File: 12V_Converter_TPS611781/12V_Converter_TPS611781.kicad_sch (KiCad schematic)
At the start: 20 parts, among them M1 CSD17308Q3T, U1 LM51561DSSR

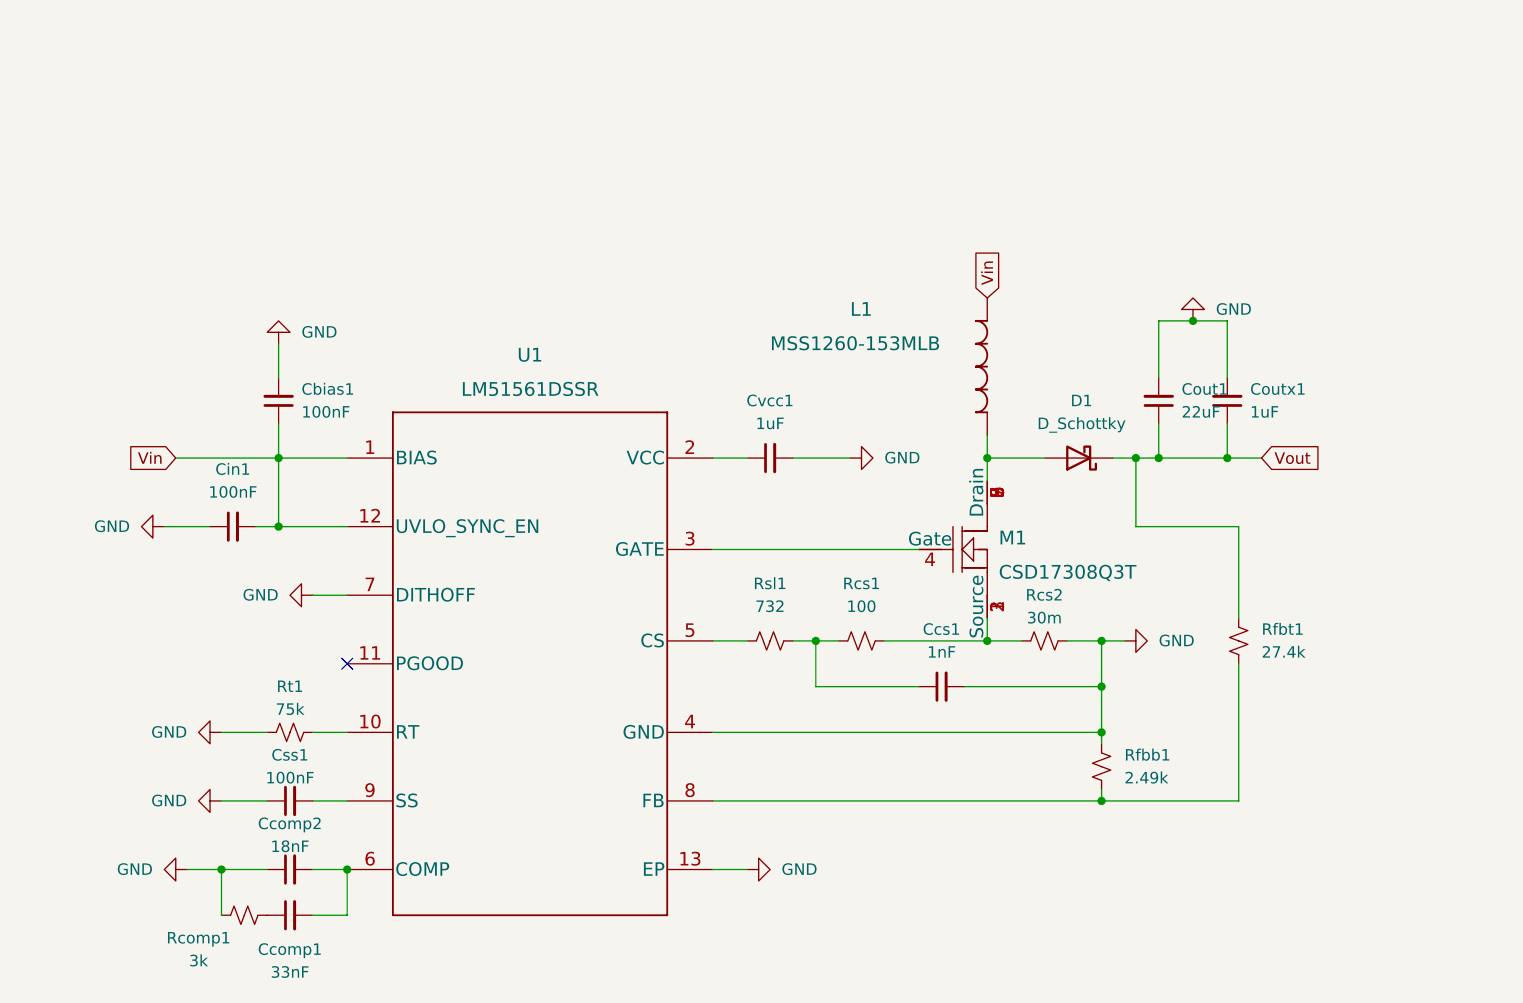
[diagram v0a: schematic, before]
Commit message: changed components
- changed inductor to be better resistance
- changed ic to be qfp instead of qfn
- changed N MOSFET to be 100V instead of 30V
- separated UVLO from Vin to allow for UVLO operation if needed (added external connect pin)
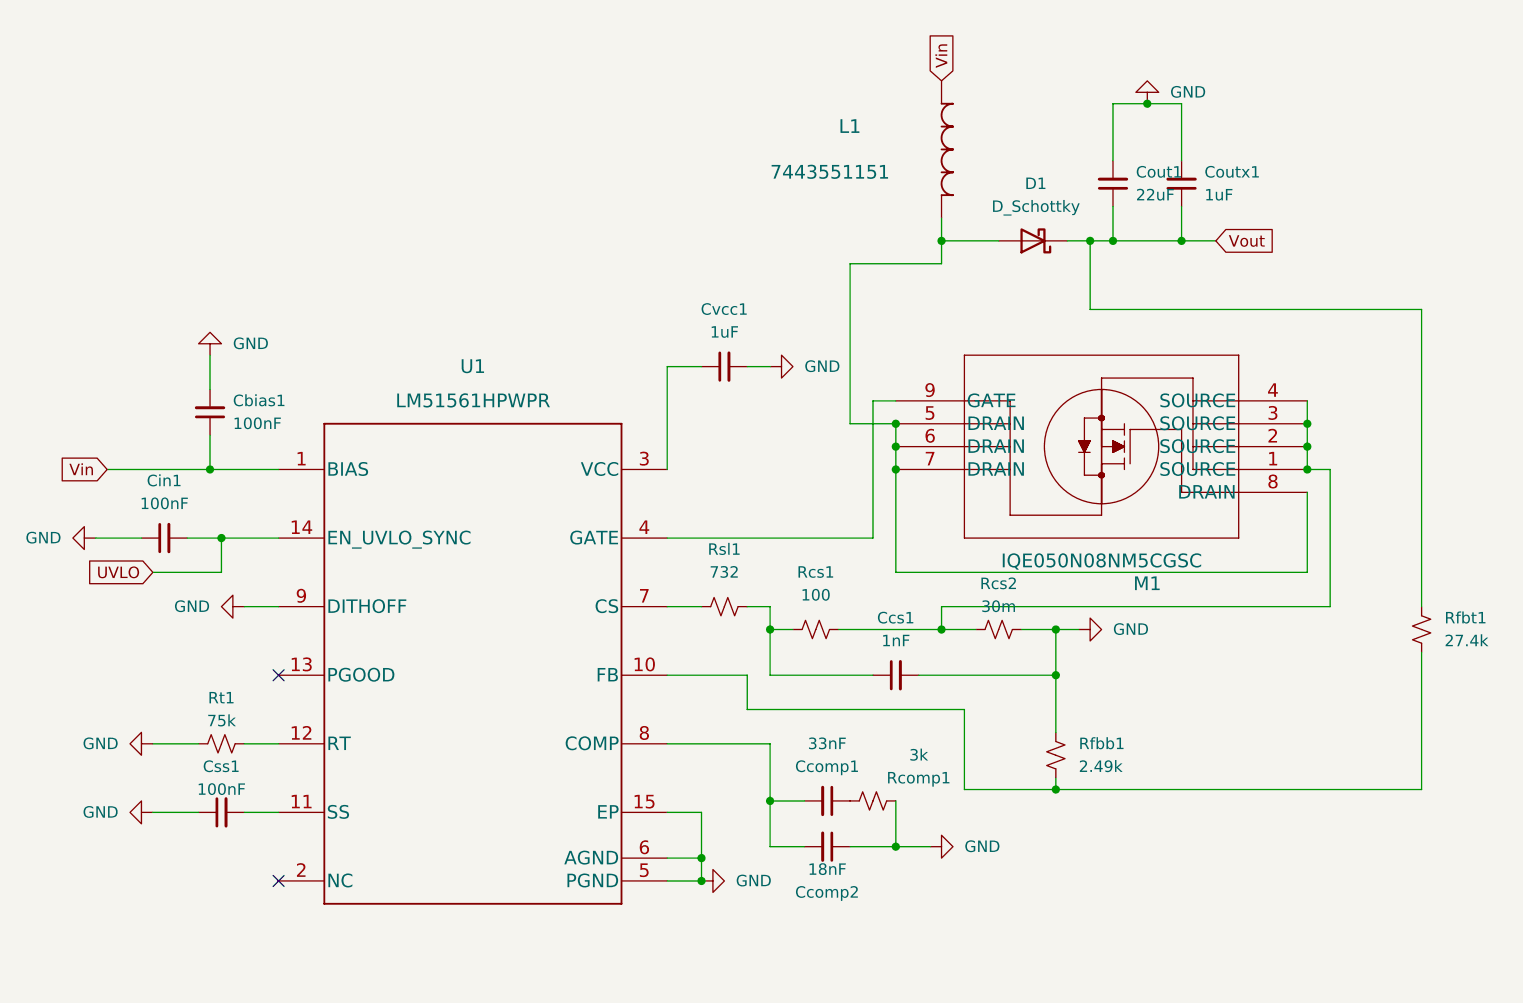
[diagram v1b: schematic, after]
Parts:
- removed L1: MSS1260-153MLB, MSS1260-153MLB:MSS1260-153MLB, symbol 2023-01-28_09-09-56:MSS1260-153MLB
- removed M1: CSD17308Q3T, CSD17308Q3T:CSD17308Q3T, symbol 2023-01-28_07-07-28:CSD17308Q3T
- removed U1: LM51561DSSR, LM51561DSSR:LM51561DSSR, symbol 2023-01-28_06-28-21:LM51561DSSR
- added L1: 7443551151, inductor:7443551151, symbol 2023-01-30_01-28-52:7443551151
- added M1: IQE050N08NM5CGSC, N MOSFET:IQE050N08NM5CGATMA1, symbol 2023-01-30_00-16-33:IQE050N08NM5CGATMA1
- added U1: LM51561HPWPR, IC:LM51561HPWPR, symbol 2023-01-29_23-53-00:LM51561HPWPR
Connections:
- net GND: now also U1.15 (EP), U1.5 (PGND), U1.6 (AGND), U1.9 (DITHOFF)
- net Vin: now also L1.2, U1.1 (BIAS); no longer Cin1.2
- net at Ccomp1.2, Ccomp2.2: now also U1.8 (COMP)
- net at Rfbb1.1, Rfbt1.1: now also U1.10 (FB)
- net at Rsl1.1: now also U1.7 (CS)
- net at Cvcc1.1: now also U1.3 (VCC)
- net at Rt1.2: now also U1.12 (RT)
- net at Css1.2: now also U1.11 (SS)
- net at D1.2 (A): now also L1.1, M1.5 (DRAIN), M1.6 (DRAIN), M1.7 (DRAIN), M1.8 (DRAIN)
- net at Rcs1.2, Rcs2.1: now also M1.1 (SOURCE), M1.2 (SOURCE), M1.3 (SOURCE), M1.4 (SOURCE)
- new net: M1.9 (GATE), U1.4 (GATE)
- new net UVLO: Cin1.2, U1.14 (EN_UVLO_SYNC)
- no-connect marks 1 -> 2
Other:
- moved on the sheet: Cbias1, Ccomp1, Ccomp2, Ccs1, Cin1, Cout1, Coutx1, Css1, Cvcc1, D1, Rcomp1, Rcs1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
